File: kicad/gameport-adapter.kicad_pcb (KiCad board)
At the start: 2 copper layers, 59.1 x 39.4 mm, 5 parts

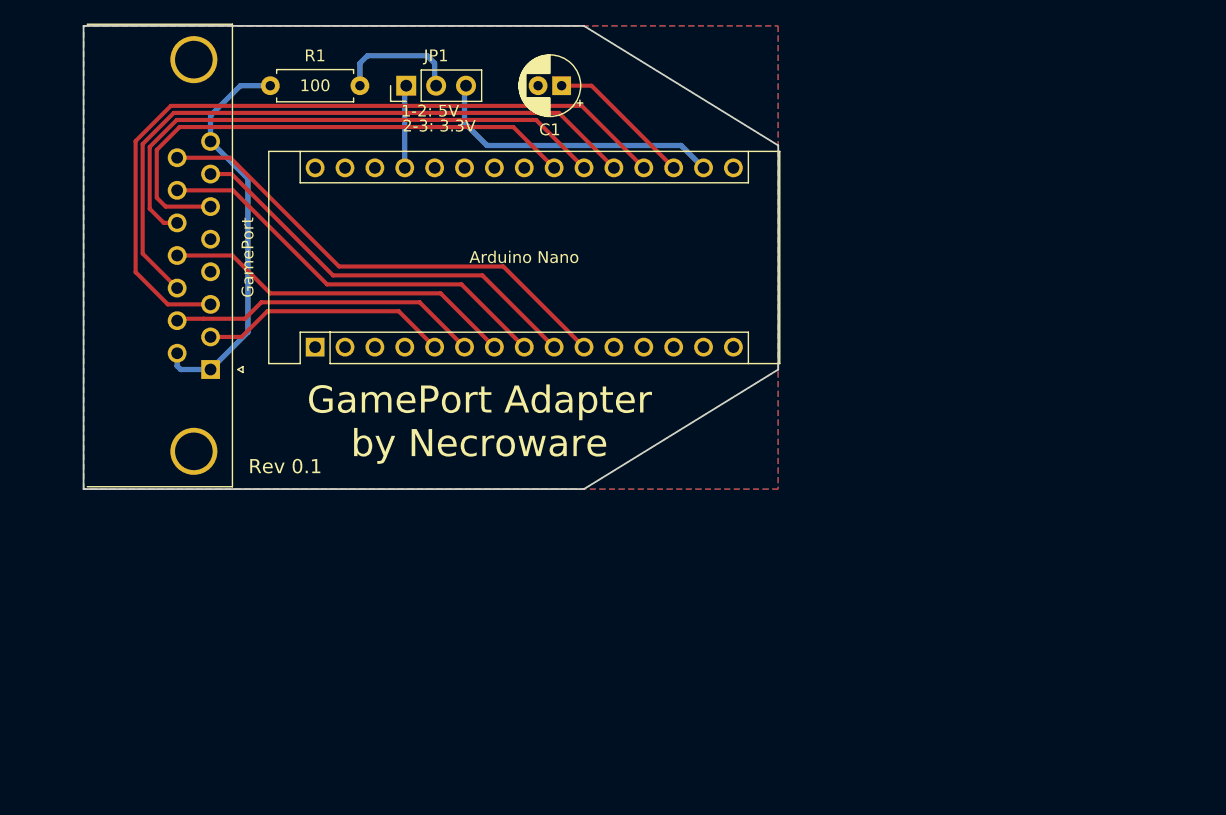
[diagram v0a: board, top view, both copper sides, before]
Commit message: Switched to Arduino Pro Micro
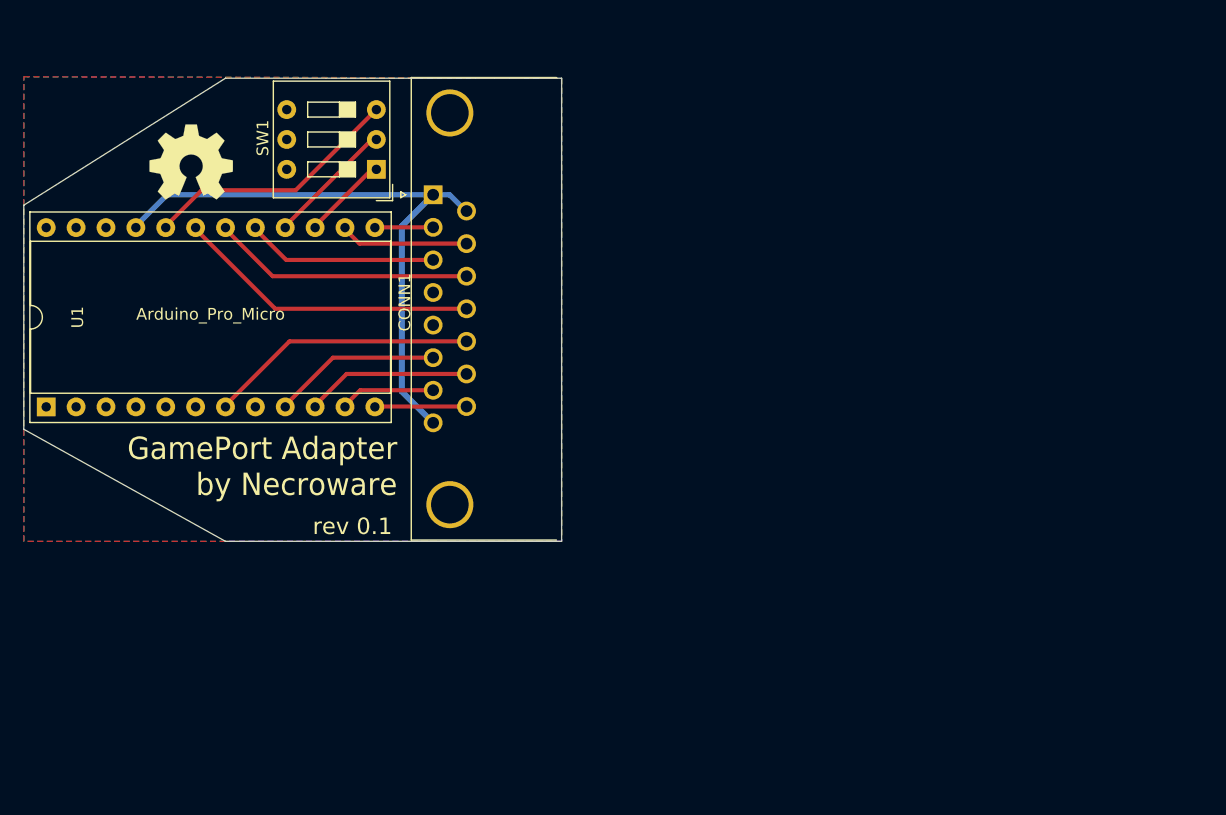
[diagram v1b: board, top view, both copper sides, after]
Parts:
- removed A1: Arduino Nano, Module:Arduino_Nano
- removed C1: 10u, Capacitor_THT:CP_Radial_D5.0mm_P2.00mm
- removed JP1: Conn_01x03, Connector_PinHeader_2.54mm:PinHeader_1x03_P2.54mm_Vertical
- removed R1: 100, Resistor_THT:R_Axial_DIN0207_L6.3mm_D2.5mm_P7.62mm_Horizontal
- added G***: LOGO, Necroware:open_hardware_logo, F.Cu at (91.1, 75.7)
- added SW1: SW_DIP_x03, Button_Switch_THT:SW_DIP_SPSTx03_Slide_9.78x9.8mm_W7.62mm_P2.54mm, F.Cu at (106.8, 76.3)
- added U1: Arduino_Pro_Micro, Package_DIP:DIP-24_W15.24mm_Socket, F.Cu at (78.7, 96.5)
- moved CONN1 24.1 mm to (111.6, 78.5), turned to 90 degrees
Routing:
- net AxisX_1: track 65.3 -> 16.4 mm
- net AxisX_2: track 56.5 -> 22.3 mm
- net MIDI_RXD: track 41.3 -> 7.93 mm
- net AxisY_1: track 45.0 -> 14.4 mm
- net Button_2: track 36.1 -> 8.21 mm
- net Net-(A1-Pad17): track 25.1 -> 0.00 mm
- net AxisY_2: track 47.6 -> 22.9 mm
- net SW3: track 0.00 -> 22.2 mm
- net Button_4: track 35.0 -> 14.2 mm
- net VCC: track 34.4 -> 51.6 mm
- net Button_1: track 21.2 -> 5.09 mm
- net Button_3: track 26.7 -> 11.0 mm
- net Net-(A1-Pad18): track 12.4 -> 0.00 mm
- net SW2: track 0.00 -> 11.0 mm
- net Net-(JP1-Pad2): track 10.7 -> 0.00 mm
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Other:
- board size 59.1 x 39.4 mm -> 45.7 x 39.4 mm
- net class Power: clearance 0.25 -> 0.35; trace_width 0.45 -> 0.5
- board text added: "1"
- board text added: "15"
- board text added: "8"
- board text added: "9"
- board text added: "rev 0.1"
- board text removed: "Rev 0.1"

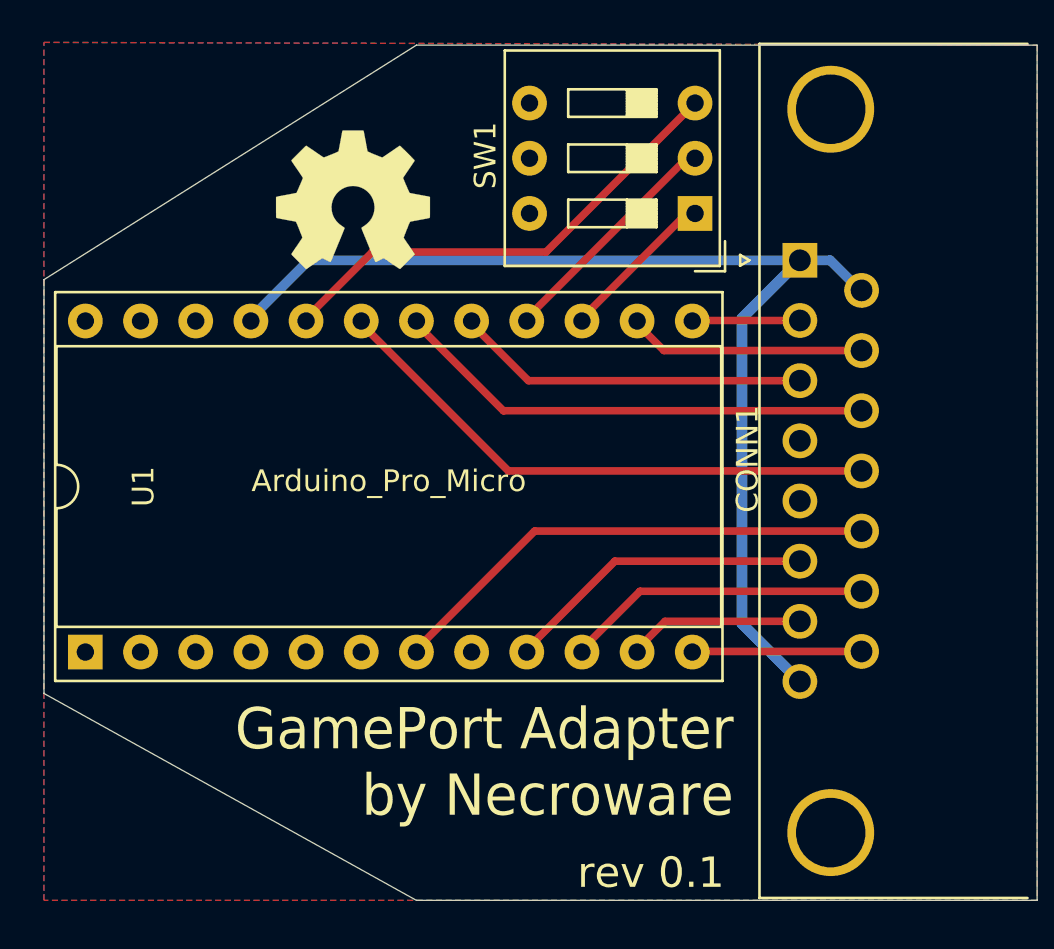
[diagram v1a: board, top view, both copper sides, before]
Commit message: Add pull-down resistors to analog pins
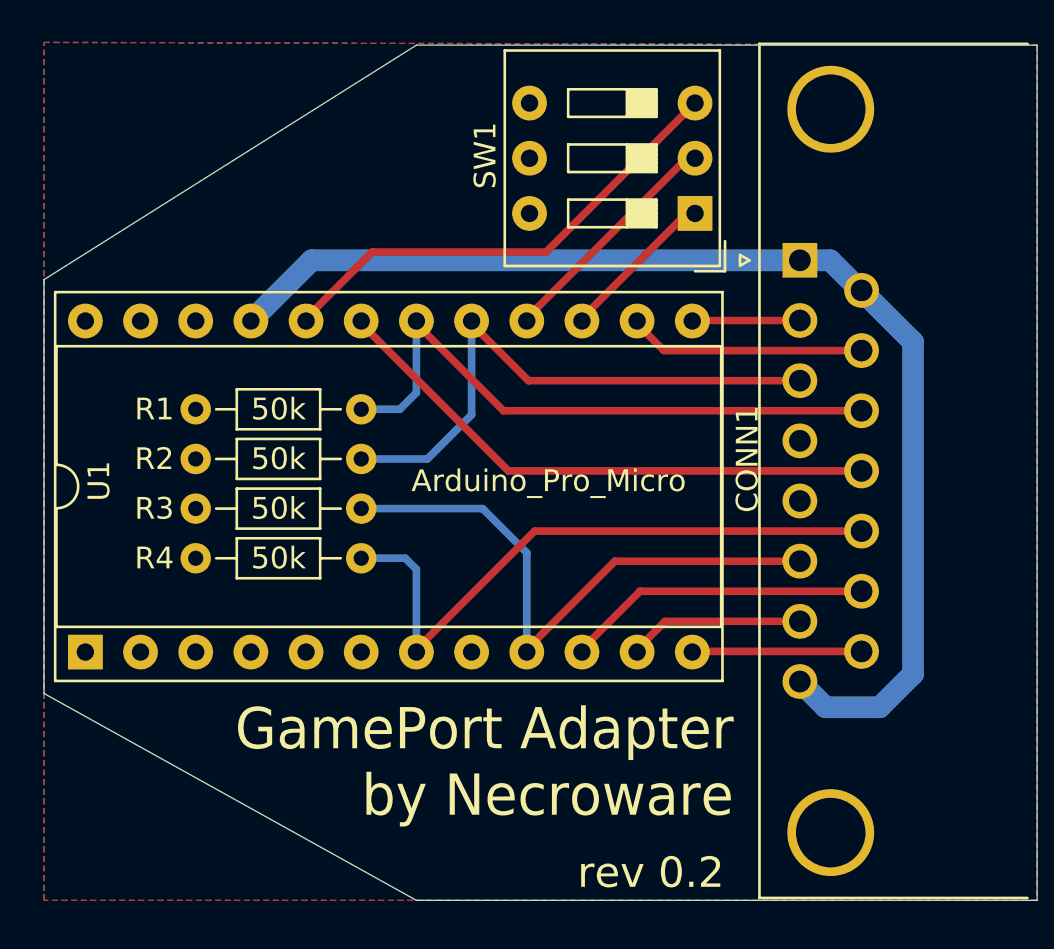
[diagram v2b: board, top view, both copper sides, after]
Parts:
- removed G***: LOGO, Necroware:open_hardware_logo
- added R1: 50k, Resistor_THT:R_Axial_DIN0204_L3.6mm_D1.6mm_P7.62mm_Horizontal, F.Cu at (91.4, 85.3)
- added R2: 50k, Resistor_THT:R_Axial_DIN0204_L3.6mm_D1.6mm_P7.62mm_Horizontal, F.Cu at (83.8, 87.6)
- added R3: 50k, Resistor_THT:R_Axial_DIN0204_L3.6mm_D1.6mm_P7.62mm_Horizontal, F.Cu at (91.4, 89.9)
- added R4: 50k, Resistor_THT:R_Axial_DIN0204_L3.6mm_D1.6mm_P7.62mm_Horizontal, F.Cu at (83.8, 92.2)
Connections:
- CONN1 pad 0: (no net) -> GND
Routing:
- net AxisY_1: track 14.4 -> 27.5 mm
- net AxisX_1: track 16.4 -> 26.6 mm
- net AxisY_2: track 22.9 -> 29.5 mm
- net AxisX_2: track 22.3 -> 28.5 mm
- net VCC: track 51.6 -> 54.8 mm
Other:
- net class Power: trace_width 0.5 -> 1
- board text added: "rev 0.2"
- board text removed: "rev 0.1"

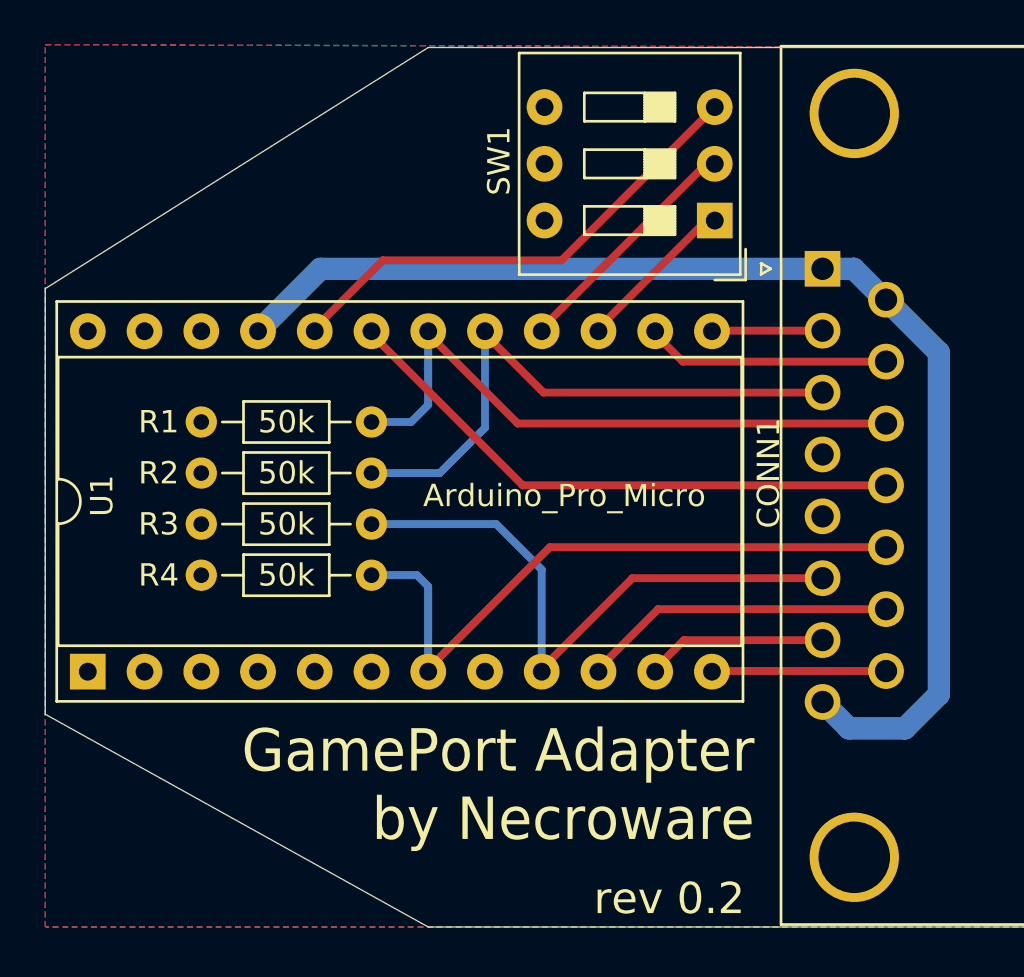
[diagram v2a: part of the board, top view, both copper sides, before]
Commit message: OSHW logo, silk layer fixes
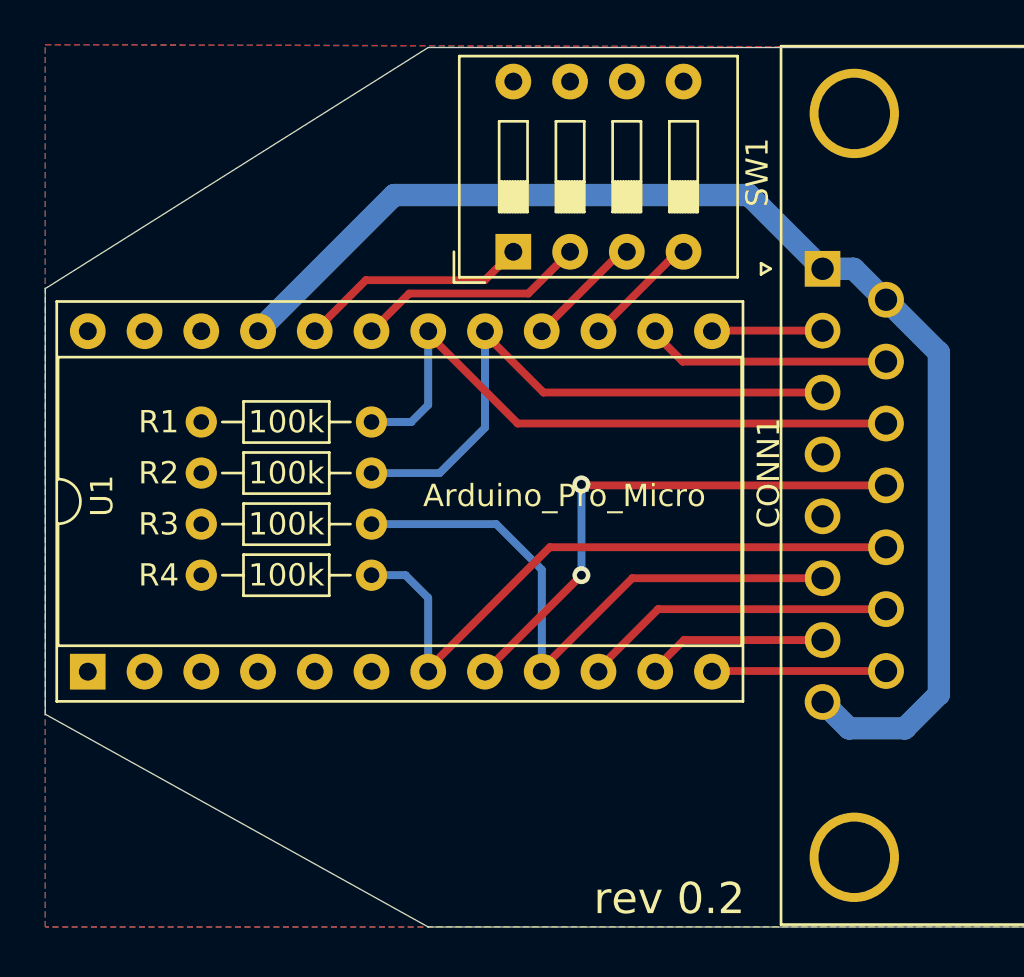
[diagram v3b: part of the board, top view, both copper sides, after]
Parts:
- added REF**: OSHW-Symbol_6.7x6mm_Copper, Symbol:OSHW-Symbol_6.7x6mm_Copper, F.Cu at (90.9, 75.2)
- R1, R2, R3, R4: value 50k -> 100k
- SW1: value SW_DIP_x03 -> SW_DIP_x04; footprint Button_Switch_THT:SW_DIP_SPSTx03_Slide_9.78x9.8mm_W7.62mm_P2.54mm -> Button_Switch_THT:SW_DIP_SPSTx04_Slide_9.78x12.34mm_W7.62mm_P2.54mm
- moved SW1 9.12 mm to (97.8, 77.7), turned to 90 degrees
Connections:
- SW1 pad 4: GND -> SW4
- U1 pad 15: SW1 -> SW4
- U1 pad 16: SW2 -> SW3
- U1 pad 19: MIDI_TXD -> SW2
- U1 pad 20: SW3 -> SW1
- U1 pad 8: (no net) -> MIDI_TXD
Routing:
- net SW3: track 22.2 -> 5.03 mm
- net SW4: track 0.00 -> 5.03 mm
- net SW1: track 7.39 -> 10.4 mm
- net VCC: track 54.8 -> 57.6 mm
- net MIDI_TXD: track 26.0 -> 23.8 mm, vias 0 -> 2
- net AxisX_2: track 28.5 -> 29.3 mm
- net SW2: track 11.0 -> 10.4 mm

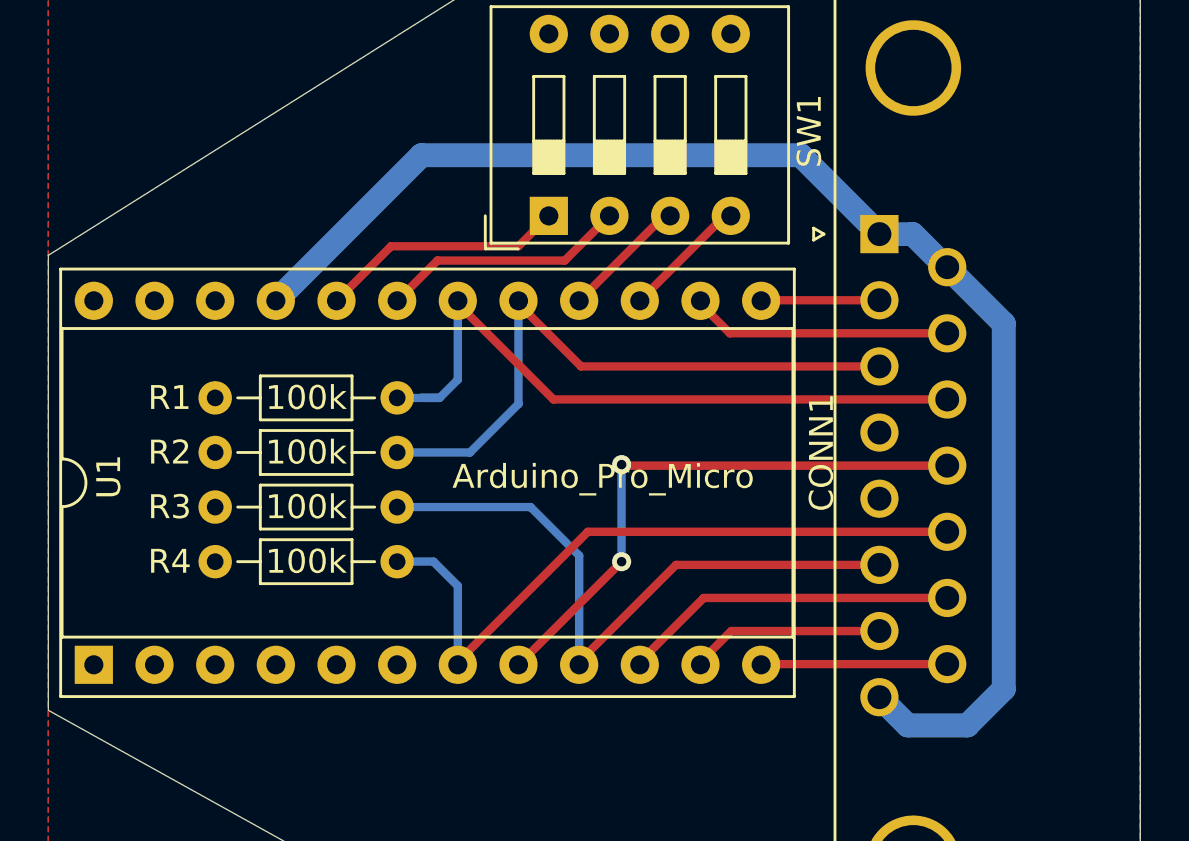
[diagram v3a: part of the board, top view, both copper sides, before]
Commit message: Move socket towards connector
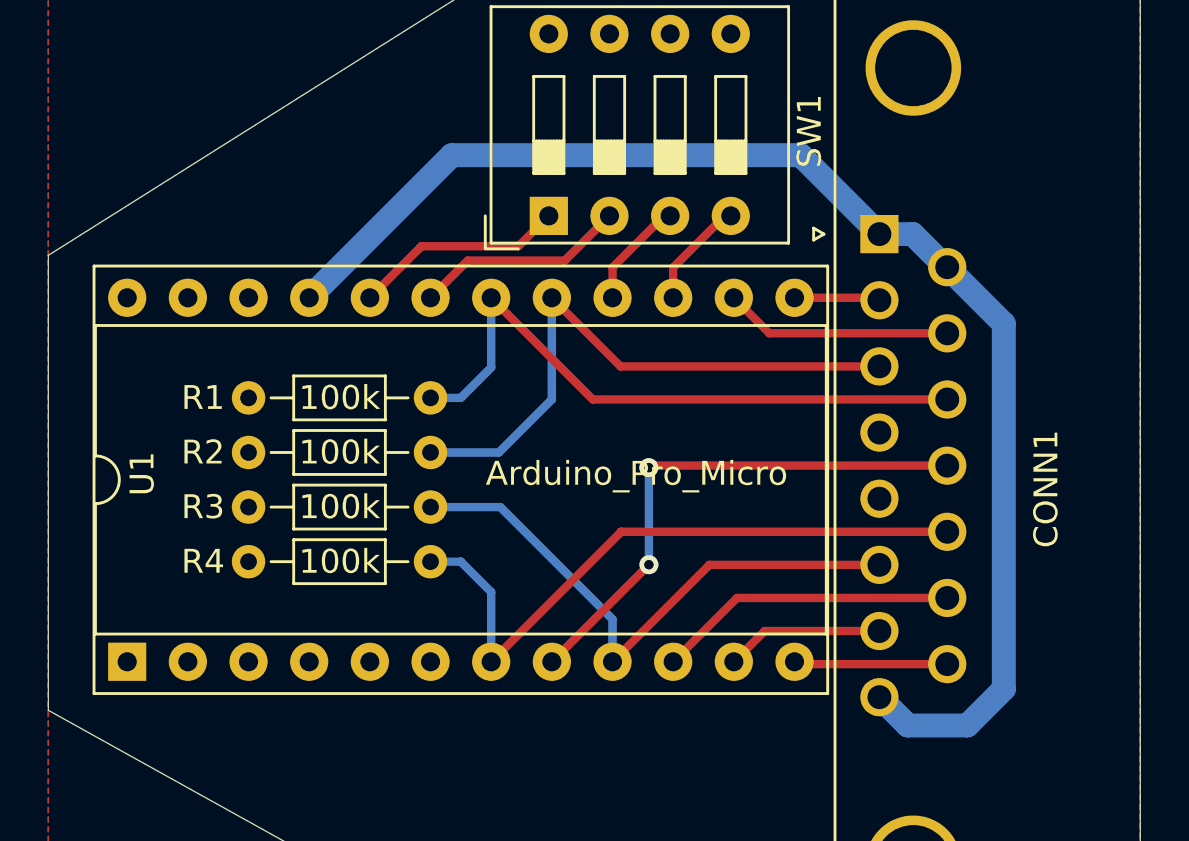
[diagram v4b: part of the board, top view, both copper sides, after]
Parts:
- moved U1 1.40 mm to (80.1, 96.4)
- moved R1 1.40 mm to (92.8, 85.3)
- moved R2 1.40 mm to (85.2, 87.6)
- moved R3 1.40 mm to (92.8, 89.9)
- moved R4 1.40 mm to (85.2, 92.2)
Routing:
- net AxisY_1: track 27.5 -> 24.3 mm
- net AxisX_2: track 29.3 -> 26.8 mm
- net AxisY_2: track 29.2 -> 27.4 mm
- net Button_2: track 8.21 -> 6.63 mm
- net Button_4: track 14.2 -> 12.6 mm
- net MIDI_RXD: track 7.93 -> 6.44 mm
- net Button_1: track 5.09 -> 3.60 mm
- net Button_3: track 11.0 -> 9.55 mm
- net AxisX_1: track 26.6 -> 25.2 mm
- net VCC: track 57.6 -> 56.1 mm
- net SW2: track 10.4 -> 8.91 mm
- net MIDI_TXD: track 23.8 -> 22.3 mm
- net SW1: track 10.4 -> 9.00 mm
- net SW4: track 5.03 -> 4.32 mm
- net SW3: track 5.03 -> 4.32 mm
